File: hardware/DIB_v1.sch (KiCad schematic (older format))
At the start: 8 parts, among them IC4 M24C32-WMN6P, J1 20-pin power socket, J17 FTDI, J3 28-pin module socket

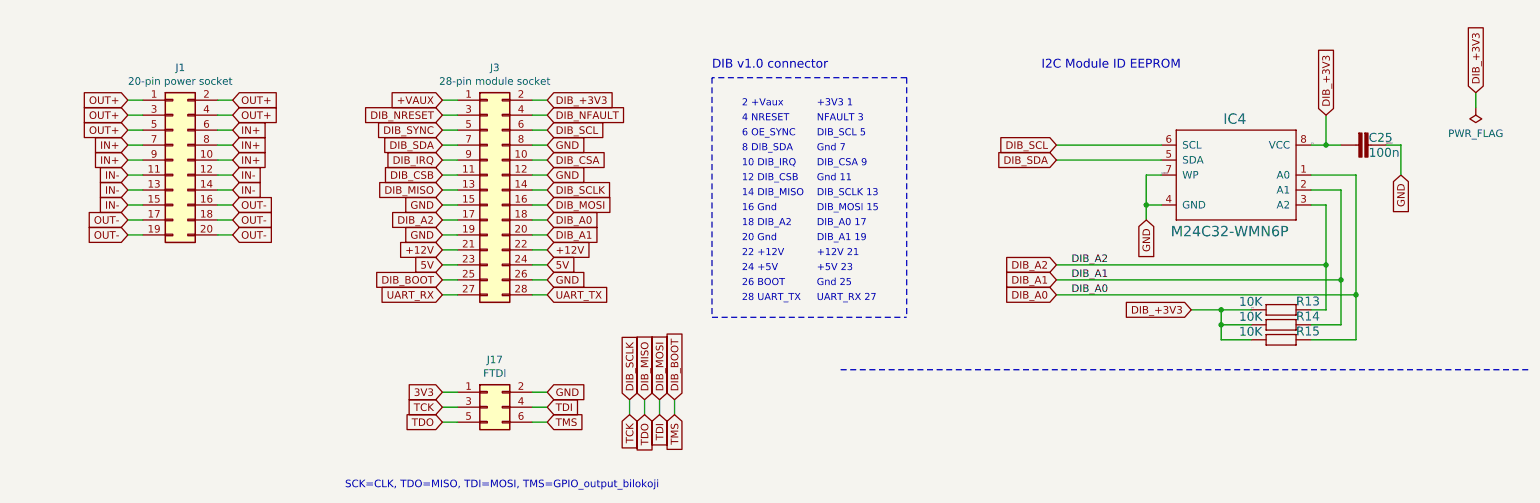
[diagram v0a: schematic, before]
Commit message: Rerouting
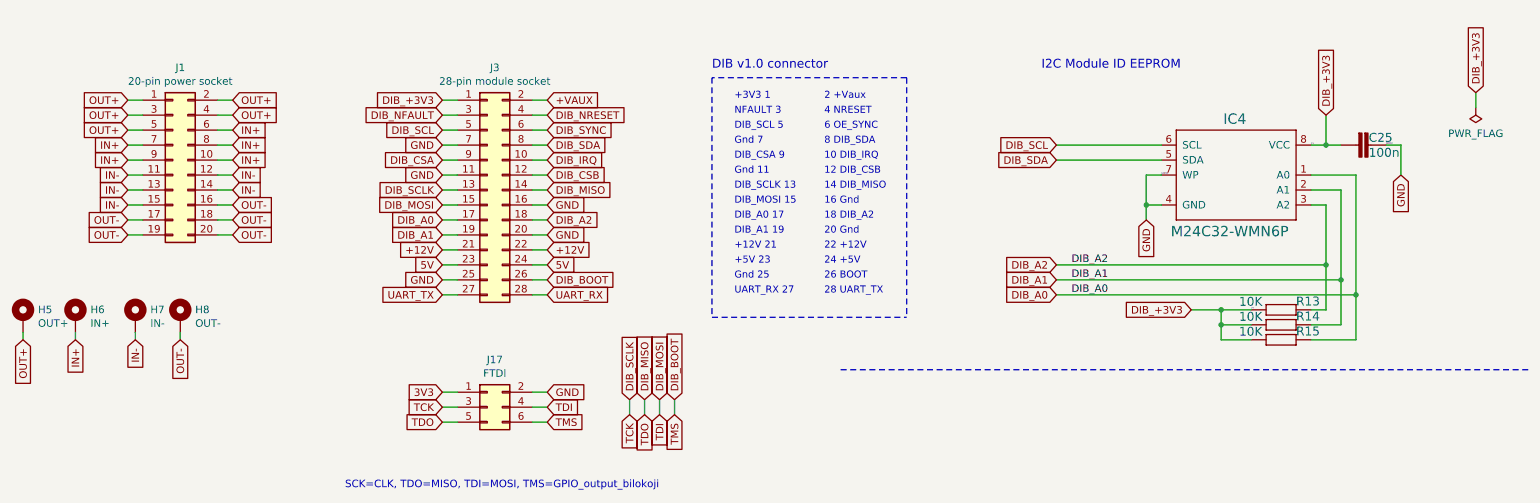
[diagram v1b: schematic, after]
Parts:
- added H5: OUT+, MountingHole:MountingHole_2.2mm_M2_Pad, symbol Mechanical:MountingHole_Pad
- added H6: IN+, MountingHole:MountingHole_2.2mm_M2_Pad, symbol Mechanical:MountingHole_Pad
- added H7: IN-, MountingHole:MountingHole_2.2mm_M2_Pad, symbol Mechanical:MountingHole_Pad
- added H8: OUT-, MountingHole:MountingHole_2.2mm_M2_Pad, symbol Mechanical:MountingHole_Pad
- J1: footprint Connector_PinSocket_2.54mm:PinSocket_2x10_P2.54mm_Horizontal -> DIB_V1:PinSocket_2x10_P2.54mm_Horizontal_DIB_V1
- J3: footprint Connector_PinHeader_2.54mm:PinHeader_2x14_P2.54mm_Horizontal -> DIB_V1:PinHeader_2x14_P2.54mm_Horizontal_DIB_V1
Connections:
- net +VAUX: now also J3.2 (Pin_2); no longer J3.1 (Pin_1)
- net DIB_+3V3: now also J3.1 (Pin_1); no longer J3.2 (Pin_2)
- net DIB_A0: now also J3.17 (Pin_17); no longer J3.18 (Pin_18)
- net DIB_A1: now also J3.19 (Pin_19); no longer J3.20 (Pin_20)
- net DIB_A2: now also J3.18 (Pin_18); no longer J3.17 (Pin_17)
- net DIB_BOOT: now also J3.26 (Pin_26); no longer J3.25 (Pin_25)
- net DIB_CSA: now also J3.9 (Pin_9); no longer J3.10 (Pin_10)
- net DIB_CSB: now also J3.12 (Pin_12); no longer J3.11 (Pin_11)
- net DIB_IRQ: now also J3.10 (Pin_10); no longer J3.9 (Pin_9)
- net DIB_MISO: now also J3.14 (Pin_14); no longer J3.13 (Pin_13)
- net DIB_MOSI: now also J3.15 (Pin_15); no longer J3.16 (Pin_16)
- net DIB_NFAULT: now also J3.3 (Pin_3); no longer J3.4 (Pin_4)
- net DIB_NRESET: now also J3.4 (Pin_4); no longer J3.3 (Pin_3)
- net DIB_SCL: now also J3.5 (Pin_5); no longer J3.6 (Pin_6)
- net DIB_SCLK: now also J3.13 (Pin_13); no longer J3.14 (Pin_14)
- net DIB_SDA: now also J3.8 (Pin_8); no longer J3.7 (Pin_7)
- net DIB_SYNC: now also J3.6 (Pin_6); no longer J3.5 (Pin_5)
- net GND: now also J3.11 (Pin_11), J3.16 (Pin_16), J3.20 (Pin_20), J3.25 (Pin_25), J3.7 (Pin_7); no longer J3.12 (Pin_12), J3.15 (Pin_15), J3.19 (Pin_19), J3.26 (Pin_26), J3.8 (Pin_8)
- net IN+: now also H6.1
- net IN-: now also H7.1
- net OUT+: now also H5.1
- net OUT-: now also H8.1
- net UART_RX: now also J3.28 (Pin_28); no longer J3.27 (Pin_27)
- net UART_TX: now also J3.27 (Pin_27); no longer J3.28 (Pin_28)
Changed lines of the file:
@@
 F 0 "J1" H 1850 2067 50  0000 C CNN
 F 1 "20-pin power socket" H 1850 1976 50  0000 C CNN
-F 2 "Connector_PinSocket_2.54mm:PinSocket_2x10_P2.54mm_Horizontal" H 1800 1450 50  0001 C CNN
+F 2 "DIB_V1:PinSocket_2x10_P2.54mm_Horizontal_DIB_V1" H 1800 1450 50  0001 C CNN
 F 3 "~" H 1800 1450 50  0001 C CNN
 	1    1800 1450
@@
 Wire Wire Line
 	2100 1550 2200 1550
-Text Notes 5600 2300 0    47   ~ 0
+Text Notes 6150 2250 0    47   ~ 0
 26 BOOT
-Text Notes 6100 1400 0    47   ~ 0
+Text Notes 5550 1350 0    47   ~ 0
 Gnd 7
-Text Notes 5600 2100 0    47   ~ 0
+Text Notes 6150 2050 0    47   ~ 0
 22 +12V
-Text Notes 5600 1800 0    47   ~ 0
+Text Notes 6150 1750 0    47   ~ 0
 16 Gnd
-Text Notes 5600 1300 0    47   ~ 0
+Text Notes 6150 1250 0    47   ~ 0
 6 OE_SYNC
-Text Notes 5600 2200 0    47   ~ 0
+Text Notes 6150 2150 0    47   ~ 0
 24 +5V
-Text Notes 6100 2200 0    47   ~ 0
+Text Notes 5550 2150 0    47   ~ 0
 +5V 23
-Text Notes 6100 2300 0    47   ~ 0
+Text Notes 5550 2250 0    47   ~ 0
 Gnd 25
-Text Notes 6100 2100 0    47   ~ 0
+Text Notes 5550 2050 0    47   ~ 0
 +12V 21
-Text Notes 5600 1500 0    47   ~ 0
+Text Notes 6150 1450 0    47   ~ 0
 10 DIB_IRQ
-Text Notes 6100 1500 0    47   ~ 0
+Text Notes 5550 1450 0    47   ~ 0
 DIB_CSA 9
-Text Notes 5600 1100 0    47   ~ 0
+Text Notes 6150 1050 0    47   ~ 0
 2 +Vaux
-Text Notes 5600 1600 0    47   ~ 0
+Text Notes 6150 1550 0    47   ~ 0
 12 DIB_CSB
-Text Notes 6100 1100 0    47   ~ 0
+Text Notes 5550 1050 0    47   ~ 0
 +3V3 1
-Text Notes 6100 1600 0    47   ~ 0
+Text Notes 5550 1550 0    47   ~ 0
 Gnd 11
-Text Notes 5600 1400 0    47   ~ 0
+Text Notes 6150 1350 0    47   ~ 0
 8 DIB_SDA
-Text Notes 6100 1300 0    47   ~ 0
+Text Notes 5550 1250 0    47   ~ 0
 DIB_SCL 5
-Text Notes 6100 2000 0    47   ~ 0
+Text Notes 5550 1950 0    47   ~ 0
 DIB_A1 19
-Text Notes 5600 1200 0    47   ~ 0
+Text Notes 6150 1150 0    47   ~ 0
 4 NRESET
-Text Notes 6100 1900 0    47   ~ 0
+Text Notes 5550 1850 0    47   ~ 0
 DIB_A0 17
-Text Notes 5600 2000 0    47   ~ 0
+Text Notes 6150 1950 0    47   ~ 0
 20 Gnd
-Text Notes 6100 1200 0    47   ~ 0
+Text Notes 5550 1150 0    47   ~ 0
 NFAULT 3
-Text Notes 5600 1700 0    47   ~ 0
+Text Notes 6150 1650 0    47   ~ 0
 14 DIB_MISO
-Text Notes 6100 1800 0    47   ~ 0
+Text Notes 5550 1750 0    47   ~ 0
 DIB_MOSI 15
-Text Notes 6100 1700 0    47   ~ 0
+Text Notes 5550 1650 0    47   ~ 0
 DIB_SCLK 13
-Text Notes 5600 1900 0    47   ~ 0
+Text Notes 6150 1850 0    47   ~ 0
 18 DIB_A2
 Wire Notes Line
 	10850 2850 6250 2850
-Text Notes 6100 2400 0    47   ~ 0
+Text Notes 5550 2350 0    47   ~ 0
 UART_RX 27
-Text Notes 5600 2400 0    47   ~ 0
+Text Notes 6150 2350 0    47   ~ 0
 28 UART_TX
 Text Notes 5400 850  0    59   ~ 0
@@
 F 0 "J3" H 3950 2467 50  0000 C CNN
 F 1 "28-pin module socket" H 3950 2376 50  0000 C CNN
-F 2 "Connector_PinHeader_2.54mm:PinHeader_2x14_P2.54mm_Horizontal" H 3900 1650 50  0001 C CNN
+F 2 "DIB_V1:PinHeader_2x14_P2.54mm_Horizontal_DIB_V1" H 3900 1650 50  0001 C CNN
 F 3 "~" H 3900 1650 50  0001 C CNN
 	1    3900 1650
 	1    0    0    -1
 $EndComp
-Text GLabel 3600 1050 0    50   Input ~ 0
+Text GLabel 4300 1050 2    50   Input ~ 0
 +VAUX
-Text GLabel 3600 1150 0    50   Input ~ 0
+Text GLabel 4300 1150 2    50   Input ~ 0
 DIB_NRESET
-Text GLabel 3600 1250 0    50   Input ~ 0
+Text GLabel 4300 1250 2    50   Input ~ 0
 DIB_SYNC
-Text GLabel 3600 1350 0    50   Input ~ 0
+Text GLabel 4300 1350 2    50   Input ~ 0
 DIB_SDA
-Text GLabel 3600 1450 0    50   Input ~ 0
+Text GLabel 4300 1450 2    50   Input ~ 0
 DIB_IRQ
-Text GLabel 3600 1550 0    50   Input ~ 0
+Text GLabel 4300 1550 2    50   Input ~ 0
 DIB_CSB
-Text GLabel 3600 1650 0    50   Input ~ 0
+Text GLabel 4300 1650 2    50   Input ~ 0
 DIB_MISO
-Text GLabel 3600 1750 0    50   Input ~ 0
-GND
-Text GLabel 3600 1850 0    50   Input ~ 0
+Text GLabel 4300 1750 2    50   Input ~ 0
+GND
+Text GLabel 4300 1850 2    50   Input ~ 0
 DIB_A2
-Text GLabel 3600 1950 0    50   Input ~ 0
+Text GLabel 4300 1950 2    50   Input ~ 0
 GND
 Text GLabel 3600 2050 0    50   Input ~ 0
@@
 Text GLabel 3600 2150 0    50   Input ~ 0
 5V
-Text GLabel 3600 2250 0    50   Input ~ 0
+Text GLabel 4300 2250 2    50   Input ~ 0
 DIB_BOOT
-Text GLabel 3600 2350 0    50   Input ~ 0
+Text GLabel 4300 2350 2    50   Input ~ 0
 UART_RX
-Text GLabel 4300 1050 2    50   Input ~ 0
+Text GLabel 3600 1050 0    50   Input ~ 0
 DIB_+3V3
-Text GLabel 4300 1150 2    50   Input ~ 0
+Text GLabel 3600 1150 0    50   Input ~ 0
 DIB_NFAULT
-Text GLabel 4300 1250 2    50   Input ~ 0
+Text GLabel 3600 1250 0    50   Input ~ 0
 DIB_SCL
-Text GLabel 4300 1350 2    50   Input ~ 0
-GND
-Text GLabel 4300 1550 2    50   Input ~ 0
-GND
-Text GLabel 4300 1450 2    50   Input ~ 0
+Text GLabel 3600 1350 0    50   Input ~ 0
+GND
+Text GLabel 3600 1550 0    50   Input ~ 0
+GND
+Text GLabel 3600 1450 0    50   Input ~ 0
 DIB_CSA
-Text GLabel 4300 1650 2    50   Input ~ 0
+Text GLabel 3600 1650 0    50   Input ~ 0
 DIB_SCLK
-Text GLabel 4300 1750 2    50   Input ~ 0
+Text GLabel 3600 1750 0    50   Input ~ 0
 DIB_MOSI
-Text GLabel 4300 1850 2    50   Input ~ 0
+Text GLabel 3600 1850 0    50   Input ~ 0
 DIB_A0
-Text GLabel 4300 1950 2    50   Input ~ 0
+Text GLabel 3600 1950 0    50   Input ~ 0
 DIB_A1
 Text GLabel 4300 2050 2    50   Input ~ 0
@@
 Text GLabel 4300 2150 2    50   Input ~ 0
 5V
-Text GLabel 4300 2250 2    50   Input ~ 0
-GND
-Text GLabel 4300 2350 2    50   Input ~ 0
+Text GLabel 3600 2250 0    50   Input ~ 0
+GND
+Text GLabel 3600 2350 0    50   Input ~ 0
 UART_TX
 Wire Wire Line
@@
 Wire Wire Line
 	10500 1000 10500 1100
+$Comp
+L Mechanical:MountingHole_Pad H5
+U 1 1 5E44E383
+P 800 2500
+F 0 "H5" H 900 2551 50  0000 L CNN
+F 1 "OUT+" H 900 2460 50  0000 L CNN
+F 2 "MountingHole:MountingHole_2.2mm_M2_Pad" H 800 2500 50  0001 C CNN
+F 3 "~" H 800 2500 50  0001 C CNN
+	1    800  2500
+	1    0    0    -1
+$EndComp
+$Comp
+L Mechanical:MountingHole_Pad H6
+U 1 1 5E44E421
+P 1150 2500
+F 0 "H6" H 1250 2551 50  0000 L CNN
+F 1 "IN+" H 1250 2460 50  0000 L CNN
+F 2 "MountingHole:MountingHole_2.2mm_M2_Pad" H 1150 2500 50  0001 C CNN
+F 3 "~" H 1150 2500 50  0001 C CNN
+	1    1150 2500
+	1    0    0    -1
+$EndComp
+$Comp
+L Mechanical:MountingHole_Pad H7
+U 1 1 5E44E45F
+P 1550 2500
+F 0 "H7" H 1650 2551 50  0000 L CNN
+F 1 "IN-" H 1650 2460 50  0000 L CNN
+F 2 "MountingHole:MountingHole_2.2mm_M2_Pad" H 1550 2500 50  0001 C CNN
+F 3 "~" H 1550 2500 50  0001 C CNN
+	1    1550 2500
+	1    0    0    -1
+$EndComp
+$Comp
+L Mechanical:MountingHole_Pad H8
+U 1 1 5E44E4A9
+P 1850 2500
+F 0 "H8" H 1950 2551 50  0000 L CNN
+F 1 "OUT-" H 1950 2460 50  0000 L CNN
+F 2 "MountingHole:MountingHole_2.2mm_M2_Pad" H 1850 2500 50  0001 C CNN
+F 3 "~" H 1850 2500 50  0001 C CNN
+	1    1850 2500
+	1    0    0    -1
+$EndComp
+Text GLabel 1850 2650 3    50   Input ~ 0
+OUT-
+Text GLabel 1550 2650 3    50   Input ~ 0
+IN-
+Text GLabel 800  2650 3    50   Input ~ 0
+OUT+
+Text GLabel 1150 2650 3    50   Input ~ 0
+IN+
+Wire Wire Line
+	800  2650 800  2600
+Wire Wire Line
+	1150 2650 1150 2600
+Wire Wire Line
+	1550 2650 1550 2600
+Wire Wire Line
+	1850 2650 1850 2600
 $EndSCHEMATC
